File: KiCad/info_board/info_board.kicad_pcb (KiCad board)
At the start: 2 copper layers, 99.1 x 99.6 mm, 30 parts, among them U1 74HC138, U2 74HC573, U3 74LS367, U4 74HC02, X1 Edge72

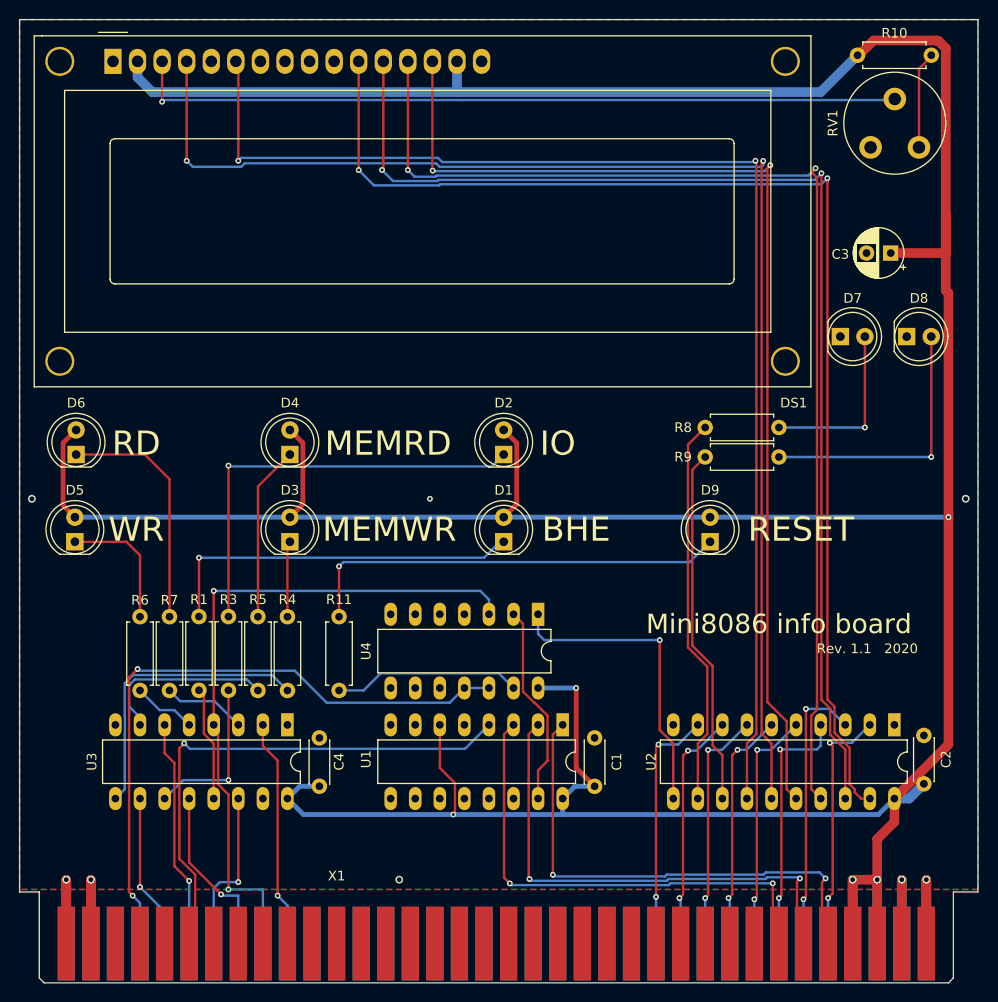
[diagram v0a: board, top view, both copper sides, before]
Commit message: Fixed main and info_board bugs.
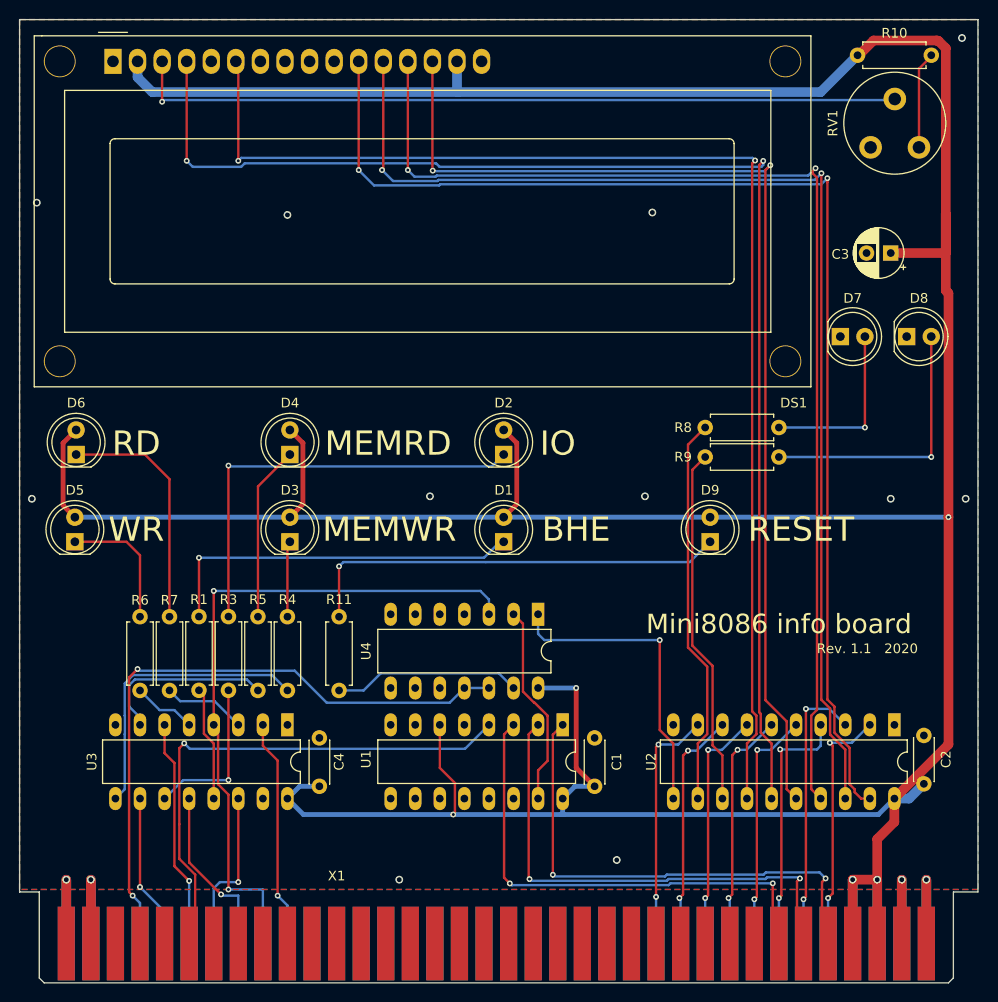
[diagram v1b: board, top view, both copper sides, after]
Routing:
- net GND: vias 8 -> 15
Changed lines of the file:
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@@
     (thickness 1.6)
     (drawings 19)
-    (tracks 443)
+    (tracks 452)
     (zones 0)
     (modules 30)
@@
     (36 B.SilkS user hide)
     (37 F.SilkS user)
-    (38 B.Mask user hide)
+    (38 B.Mask user)
     (39 F.Mask user hide)
     (40 Dwgs.User user hide)
@@
     (46 B.CrtYd user hide)
     (47 F.CrtYd user hide)
-    (48 B.Fab user)
+    (48 B.Fab user hide)
     (49 F.Fab user hide)
   )
   (setup
-    (last_trace_width 1)
+    (last_trace_width 0.25)
     (user_trace_width 0.25)
     (user_trace_width 0.5)
@@
     (mod_text_size 1 1)
     (mod_text_width 0.15)
-    (pad_size 2.4 1.3)
-    (pad_drill 0.8)
+    (pad_size 3.3 3.3)
+    (pad_drill 3.1)
     (pad_to_mask_clearance 0.05)
     (aux_axis_origin 0 0)
@@
       (effects (font (size 1 1) (thickness 0.1)))
     )
-    (pad "" thru_hole circle (at 69.5 0) (size 3 3) (drill 2.5) (layers *.Cu *.Mask))
-    (pad "" thru_hole circle (at 69.49948 31.0007) (size 3 3) (drill 2.5) (layers *.Cu *.Mask))
-    (pad "" thru_hole circle (at -5.4991 31.0007) (size 3 3) (drill 2.5) (layers *.Cu *.Mask))
-    (pad "" thru_hole circle (at -5.4991 0) (size 3 3) (drill 2.5) (layers *.Cu *.Mask))
+    (pad "" thru_hole circle (at 69.5 0) (size 3.3 3.3) (drill 3.1) (layers *.Cu *.Mask))
+    (pad "" thru_hole circle (at 69.49948 31.0007) (size 3.3 3.3) (drill 3.1) (layers *.Cu *.Mask))
+    (pad "" thru_hole circle (at -5.4991 31.0007) (size 3.3 3.3) (drill 3.1) (layers *.Cu *.Mask))
+    (pad "" thru_hole circle (at -5.4991 0) (size 3.3 3.3) (drill 3.1) (layers *.Cu *.Mask))
     (pad 16 thru_hole oval (at 38.1 0) (size 1.8 2.6) (drill 1.2) (layers *.Cu *.Mask)
       (net 1 GND))
@@
   (via (at 77.47 100.33) (size 0.8) (drill 0.5) (layers F.Cu B.Cu) (net 1))
   (via (at 173.99 100.33) (size 0.8) (drill 0.5) (layers F.Cu B.Cu) (net 1))
-  (via (at 118.618 100.33) (size 0.6) (drill 0.3) (layers F.Cu B.Cu) (net 1))
+  (via (at 118.618 100.076) (size 0.8) (drill 0.5) (layers F.Cu B.Cu) (net 1))
+  (via (at 140.843 100.076) (size 0.8) (drill 0.5) (layers F.Cu B.Cu) (net 1))
+  (via (at 166.243 100.33) (size 0.8) (drill 0.5) (layers F.Cu B.Cu) (net 1))
+  (via (at 77.978 69.723) (size 0.8) (drill 0.5) (layers F.Cu B.Cu) (net 1))
+  (via (at 173.609 52.705) (size 0.8) (drill 0.5) (layers F.Cu B.Cu) (net 1))
+  (via (at 141.605 70.739) (size 0.8) (drill 0.5) (layers F.Cu B.Cu) (net 1))
+  (via (at 103.886 70.993) (size 0.8) (drill 0.5) (layers F.Cu B.Cu) (net 1))
+  (via (at 137.922 137.668) (size 0.8) (drill 0.5) (layers F.Cu B.Cu) (net 1))
   (segment (start 164.846 146.304) (end 164.846 139.7) (width 1) (layer B.Cu) (net 2))
   (segment (start 162.306 146.304) (end 162.306 139.7) (width 1) (layer B.Cu) (net 2))
@@
   (segment (start 118.872 55.118) (end 118.872 66.38254) (width 0.25) (layer F.Cu) (net 53))
   (via (at 118.90047 66.41101) (size 0.6) (drill 0.3) (layers F.Cu B.Cu) (net 53))
-  (segment (start 155.48899 123.334118) (end 153.497 121.342128) (width 0.25) (layer F.Cu) (net 53))
   (via (at 153.797 65.853156) (size 0.6) (drill 0.3) (layers F.Cu B.Cu) (net 53))
   (segment (start 118.90047 66.41101) (end 118.959482 66.470022) (width 0.25) (layer B.Cu) (net 53))
+  (segment (start 153.180134 66.470022) (end 153.797 65.853156) (width 0.25) (layer B.Cu) (net 53))
+  (segment (start 118.959482 66.470022) (end 153.180134 66.470022) (width 0.25) (layer B.Cu) (net 53))
+  (segment (start 155.48899 123.334118) (end 153.289 121.134128) (width 0.25) (layer F.Cu) (net 53))
+  (segment (start 156.464 131.318) (end 155.48899 130.34299) (width 0.25) (layer F.Cu) (net 53))
+  (segment (start 153.289 66.361156) (end 153.797 65.853156) (width 0.25) (layer F.Cu) (net 53))
+  (segment (start 153.289 121.134128) (end 153.289 66.361156) (width 0.25) (layer F.Cu) (net 53))
   (segment (start 155.48899 130.34299) (end 155.48899 123.334118) (width 0.25) (layer F.Cu) (net 53))
-  (segment (start 153.180134 66.470022) (end 153.797 65.853156) (width 0.25) (layer B.Cu) (net 53))
-  (segment (start 156.464 131.318) (end 155.48899 130.34299) (width 0.25) (layer F.Cu) (net 53))
-  (segment (start 153.497001 66.153155) (end 153.797 65.853156) (width 0.25) (layer F.Cu) (net 53))
-  (segment (start 118.959482 66.470022) (end 153.180134 66.470022) (width 0.25) (layer B.Cu) (net 53))
-  (segment (start 153.497 121.342128) (end 153.497001 66.153155) (width 0.25) (layer F.Cu) (net 53))
   (segment (start 158.17163 66.690708) (end 158.17163 66.465393) (width 0.25) (layer F.Cu) (net 54))
   (via (at 158.471629 66.165394) (size 0.6) (drill 0.3) (layers F.Cu B.Cu) (net 54))
@@
   (segment (start 98.806 55.372) (end 98.552 55.118) (width 0.25) (layer F.Cu) (net 57))
   (segment (start 98.806 65.395) (end 98.806 55.372) (width 0.25) (layer F.Cu) (net 57))
+  (segment (start 151.953739 65.095001) (end 152.223308 65.36457) (width 0.25) (layer B.Cu) (net 57))
+  (segment (start 98.806 65.395) (end 99.105999 65.095001) (width 0.25) (layer B.Cu) (net 57))
+  (via (at 152.223308 65.36457) (size 0.6) (drill 0.3) (layers F.Cu B.Cu) (net 57))
+  (segment (start 99.105999 65.095001) (end 151.953739 65.095001) (width 0.25) (layer B.Cu) (net 57))
+  (segment (start 152.35901 124.651862) (end 152.35901 122.744138) (width 0.25) (layer F.Cu) (net 57))
+  (segment (start 152.35901 122.744138) (end 151.923309 122.308437) (width 0.25) (layer F.Cu) (net 57))
+  (segment (start 151.384 131.318) (end 151.384 125.626872) (width 0.25) (layer F.Cu) (net 57))
   (segment (start 151.384 125.626872) (end 152.35901 124.651862) (width 0.25) (layer F.Cu) (net 57))
-  (segment (start 152.35901 65.490308) (end 152.263553 65.394851) (width 0.25) (layer F.Cu) (net 57))
-  (segment (start 152.35901 124.651862) (end 152.35901 65.490308) (width 0.25) (layer F.Cu) (net 57))
-  (via (at 152.263553 65.394851) (size 0.6) (drill 0.3) (layers F.Cu B.Cu) (net 57))
-  (segment (start 151.384 131.318) (end 151.384 125.626872) (width 0.25) (layer F.Cu) (net 57))
-  (segment (start 152.126404 65.532) (end 152.263553 65.394851) (width 0.25) (layer B.Cu) (net 57))
-  (segment (start 119.888 65.532) (end 152.126404 65.532) (width 0.25) (layer B.Cu) (net 57))
-  (segment (start 119.451001 65.095001) (end 119.888 65.532) (width 0.25) (layer B.Cu) (net 57))
-  (segment (start 98.806 65.395) (end 99.105999 65.095001) (width 0.25) (layer B.Cu) (net 57))
-  (segment (start 99.105999 65.095001) (end 119.451001 65.095001) (width 0.25) (layer B.Cu) (net 57))
+  (segment (start 151.923309 122.308437) (end 151.923309 65.664569) (width 0.25) (layer F.Cu) (net 57))
+  (segment (start 151.923309 65.664569) (end 152.223308 65.36457) (width 0.25) (layer F.Cu) (net 57))
   (via (at 93.472 65.395) (size 0.6) (drill 0.3) (layers F.Cu B.Cu) (net 58))
   (segment (start 93.472 65.395) (end 93.472 55.118) (width 0.25) (layer F.Cu) (net 58))
-  (segment (start 153.924 125.626872) (end 152.898002 124.600874) (width 0.25) (layer F.Cu) (net 58))
-  (segment (start 152.898002 124.600874) (end 152.898002 65.573775) (width 0.25) (layer F.Cu) (net 58))
-  (segment (start 152.898002 65.573775) (end 153.063451 65.408326) (width 0.25) (layer F.Cu) (net 58))
   (via (at 153.063451 65.408326) (size 0.6) (drill 0.3) (layers F.Cu B.Cu) (net 58))
-  (segment (start 153.924 131.318) (end 153.924 125.626872) (width 0.25) (layer F.Cu) (net 58))
   (segment (start 153.063451 65.83259) (end 153.063451 65.408326) (width 0.25) (layer B.Cu) (net 58))
   (segment (start 119.614011 66.020011) (end 152.87603 66.020011) (width 0.25) (layer B.Cu) (net 58))
@@
   (segment (start 119.253 65.659) (end 119.614011 66.020011) (width 0.25) (layer B.Cu) (net 58))
   (segment (start 99.467002 65.659) (end 119.253 65.659) (width 0.25) (layer B.Cu) (net 58))
+  (segment (start 152.654 122.402717) (end 152.654 65.817777) (width 0.25) (layer F.Cu) (net 58))
+  (segment (start 153.924 125.626872) (end 152.809021 124.511893) (width 0.25) (layer F.Cu) (net 58))
+  (segment (start 153.924 131.318) (end 153.924 125.626872) (width 0.25) (layer F.Cu) (net 58))
+  (segment (start 152.654 65.817777) (end 153.063451 65.408326) (width 0.25) (layer F.Cu) (net 58))
+  (segment (start 152.809021 124.511893) (end 152.809021 122.557738) (width 0.25) (layer F.Cu) (net 58))
+  (segment (start 152.809021 122.557738) (end 152.654 122.402717) (width 0.25) (layer F.Cu) (net 58))
   (segment (start 147.27901 124.651862) (end 147.27901 117.68801) (width 0.25) (layer F.Cu) (net 59))
   (segment (start 146.304 131.318) (end 146.304 125.626872) (width 0.25) (layer F.Cu) (net 59))

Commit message: Migration from KiCad 5 to KiCad 7
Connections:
- net /LCD/~CS_LCDREG renamed /LCD/~{CS_LCDREG}
- net ~BHE renamed ~{BHE}
- net ~IO renamed ~{IO}
- net ~IO_DBG renamed ~{IO_DBG}
- net ~MEMRD renamed ~{MEMRD}
- net ~MEMWR renamed ~{MEMWR}
- net ~RD renamed ~{RD}
- net ~WR renamed ~{WR}
- U1 pad 10: Net-(U1-Pad10) -> unconnected-(U1-O5-Pad10)
- U1 pad 11: Net-(U1-Pad11) -> unconnected-(U1-O4-Pad11)
- U1 pad 12: Net-(U1-Pad12) -> unconnected-(U1-O3-Pad12)
- U1 pad 13: Net-(U1-Pad13) -> unconnected-(U1-O2-Pad13)
- U1 pad 14: Net-(U1-Pad14) -> unconnected-(U1-O1-Pad14)
- U1 pad 7: Net-(U1-Pad7) -> unconnected-(U1-O7-Pad7)
- U1 pad 9: Net-(U1-Pad9) -> unconnected-(U1-O6-Pad9)
- U4 pad 10: Net-(U4-Pad10) -> unconnected-(U4-Pad10)
- U4 pad 4: Net-(U4-Pad4) -> unconnected-(U4-Pad4)
- X1 pad 10: Net-(X1-Pad10) -> unconnected-(X1-A5-Pad10)
- X1 pad 11: Net-(X1-Pad11) -> unconnected-(X1-A6-Pad11)
- X1 pad 12: Net-(X1-Pad12) -> unconnected-(X1-A7-Pad12)
- X1 pad 13: Net-(X1-Pad13) -> unconnected-(X1-A8-Pad13)
- X1 pad 14: Net-(X1-Pad14) -> unconnected-(X1-A9-Pad14)
- X1 pad 15: Net-(X1-Pad15) -> unconnected-(X1-A10-Pad15)
- X1 pad 16: Net-(X1-Pad16) -> unconnected-(X1-A11-Pad16)
- X1 pad 17: Net-(X1-Pad17) -> unconnected-(X1-A12-Pad17)
- X1 pad 18: Net-(X1-Pad18) -> unconnected-(X1-A13-Pad18)
- X1 pad 19: Net-(X1-Pad19) -> unconnected-(X1-A14-Pad19)
- X1 pad 20: Net-(X1-Pad20) -> unconnected-(X1-A15-Pad20)
- X1 pad 21: Net-(X1-Pad21) -> unconnected-(X1-A16-Pad21)
- X1 pad 22: Net-(X1-Pad22) -> unconnected-(X1-A17-Pad22)
- X1 pad 23: Net-(X1-Pad23) -> unconnected-(X1-A18-Pad23)
- X1 pad 24: Net-(X1-Pad24) -> unconnected-(X1-A19-Pad24)
- X1 pad 25: Net-(X1-Pad25) -> unconnected-(X1-N/C-Pad25)
- X1 pad 26: Net-(X1-Pad26) -> unconnected-(X1-~{VGA_IO}-Pad26)
- X1 pad 27: Net-(X1-Pad27) -> unconnected-(X1-~{VGA_MEM}-Pad27)
- X1 pad 28: Net-(X1-Pad28) -> unconnected-(X1-RDY1-Pad28)
- X1 pad 29: Net-(X1-Pad29) -> unconnected-(X1-RDY2-Pad29)
- X1 pad 30: Net-(X1-Pad30) -> unconnected-(X1-PCLK-Pad30)
- X1 pad 32: Net-(X1-Pad32) -> unconnected-(X1-NMI-Pad32)
- X1 pad 33: Net-(X1-Pad33) -> unconnected-(X1-TMR2-Pad33)
- X1 pad 34: Net-(X1-Pad34) -> unconnected-(X1-N/C-Pad34)
- X1 pad 49: Net-(X1-Pad49) -> unconnected-(X1-D8-Pad49)
- X1 pad 50: Net-(X1-Pad50) -> unconnected-(X1-D9-Pad50)
- X1 pad 51: Net-(X1-Pad51) -> unconnected-(X1-D10-Pad51)
- X1 pad 52: Net-(X1-Pad52) -> unconnected-(X1-D11-Pad52)
- X1 pad 53: Net-(X1-Pad53) -> unconnected-(X1-D12-Pad53)
- X1 pad 54: Net-(X1-Pad54) -> unconnected-(X1-D13-Pad54)
- X1 pad 55: Net-(X1-Pad55) -> unconnected-(X1-D14-Pad55)
- X1 pad 56: Net-(X1-Pad56) -> unconnected-(X1-D15-Pad56)
- X1 pad 57: Net-(X1-Pad57) -> unconnected-(X1-IRQ1-Pad57)
- X1 pad 58: Net-(X1-Pad58) -> unconnected-(X1-IRQ3-Pad58)
- X1 pad 59: Net-(X1-Pad59) -> unconnected-(X1-IRQ4-Pad59)
- X1 pad 60: Net-(X1-Pad60) -> unconnected-(X1-IRQ5-Pad60)
- X1 pad 61: Net-(X1-Pad61) -> unconnected-(X1-IRQ6-Pad61)
- X1 pad 62: Net-(X1-Pad62) -> unconnected-(X1-IRQ7-Pad62)
- X1 pad 70: Net-(X1-Pad70) -> unconnected-(X1-N/C-Pad70)
- X1 pad 8: Net-(X1-Pad8) -> unconnected-(X1-A3-Pad8)
- X1 pad 9: Net-(X1-Pad9) -> unconnected-(X1-A4-Pad9)
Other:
- net class Default removed
